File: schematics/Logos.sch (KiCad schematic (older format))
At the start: 10 parts

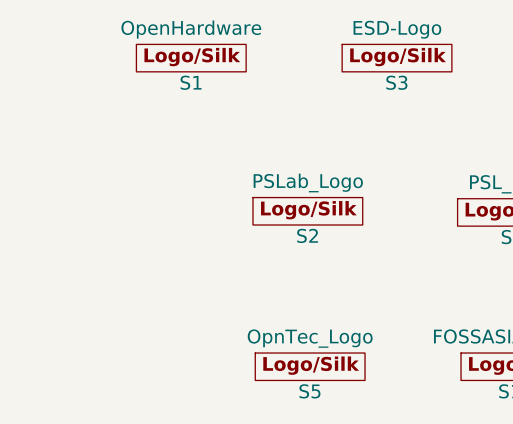
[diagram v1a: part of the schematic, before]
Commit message: feat: added ws2812b led
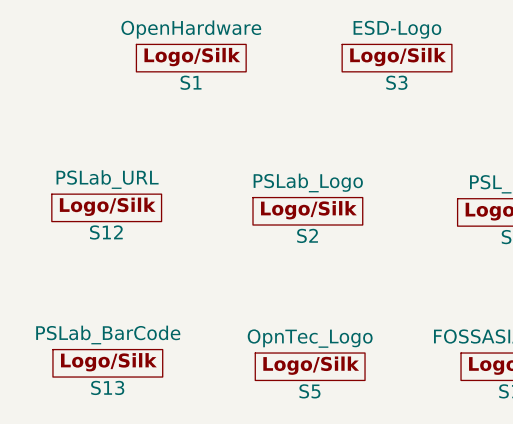
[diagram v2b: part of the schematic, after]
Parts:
- added S12: PSLab_URL, Custom_Components:PSLab_URL, symbol PSLab:Logos
- added S13: PSLab_BarCode, Custom_Components:Barcode, symbol PSLab:Logos
- S1: footprint Symbols:OSHW-Logo_5.7x6mm_SilkScreen -> Symbol:OSHW-Logo_5.7x6mm_SilkScreen
- S3: footprint Symbols:ESD-Logo_6.6x6mm_SilkScreen -> Symbol:ESD-Logo_6.6x6mm_SilkScreen
- S5: footprint Custom_Components:OpnTec_Logo -> Custom_Components:OpnTec_Logo_L
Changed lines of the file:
@@
 F 0 "S1" H 4560 2725 60  0000 C CNN
 F 1 "OpenHardware" H 4560 2965 60  0000 C CNN
-F 2 "Symbols:OSHW-Logo_5.7x6mm_SilkScreen" H 4560 2845 60  0001 C CNN
+F 2 "Symbol:OSHW-Logo_5.7x6mm_SilkScreen" H 4560 2845 60  0001 C CNN
 F 3 "" H 4560 2845 60  0001 C CNN
 	1    4560 2845
@@
 F 0 "S3" H 5460 2725 60  0000 C CNN
 F 1 "ESD-Logo" H 5460 2965 60  0000 C CNN
-F 2 "Symbols:ESD-Logo_6.6x6mm_SilkScreen" H 5460 2845 60  0001 C CNN
+F 2 "Symbol:ESD-Logo_6.6x6mm_SilkScreen" H 5460 2845 60  0001 C CNN
 F 3 "" H 5460 2845 60  0001 C CNN
 	1    5460 2845
@@
 F 0 "S5" H 5080 4075 60  0000 C CNN
 F 1 "OpnTec_Logo" H 5080 4315 60  0000 C CNN
-F 2 "Custom_Components:OpnTec_Logo" H 5080 4195 60  0001 C CNN
+F 2 "Custom_Components:OpnTec_Logo_L" H 5080 4195 60  0001 C CNN
 F 3 "" H 5080 4195 60  0001 C CNN
 	1    5080 4195
@@
 	1    0    0    -1
 $EndComp
+$Comp
+L PSLab:Logos S13
+U 1 1 5F7D714E
+P 4195 4180
+F 0 "S13" H 4195 4060 60  0000 C CNN
+F 1 "PSLab_BarCode" H 4195 4300 60  0000 C CNN
+F 2 "Custom_Components:Barcode" H 4195 4180 60  0001 C CNN
+F 3 "" H 4195 4180 60  0001 C CNN
+	1    4195 4180
+	1    0    0    -1
+$EndComp
+$Comp
+L PSLab:Logos S12
+U 1 1 5F7D7A3D
+P 4190 3500
+F 0 "S12" H 4190 3380 60  0000 C CNN
+F 1 "PSLab_URL" H 4190 3620 60  0000 C CNN
+F 2 "Custom_Components:PSLab_URL" H 4190 3500 60  0001 C CNN
+F 3 "" H 4190 3500 60  0001 C CNN
+	1    4190 3500
+	1    0    0    -1
+$EndComp

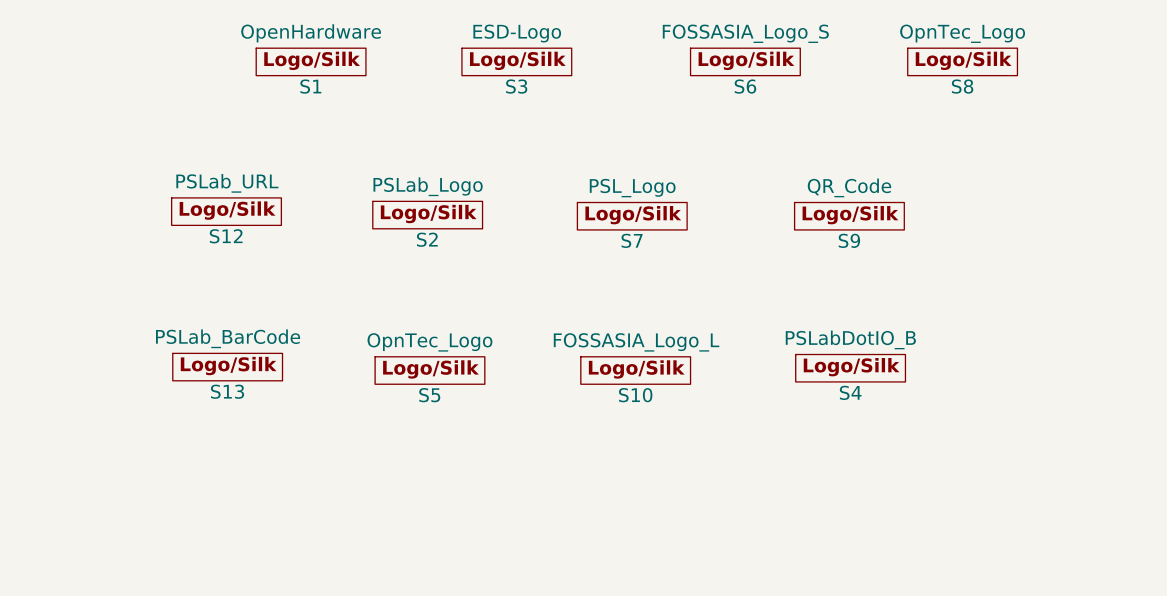
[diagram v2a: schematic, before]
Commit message: feat: enhanced bottom silk screen
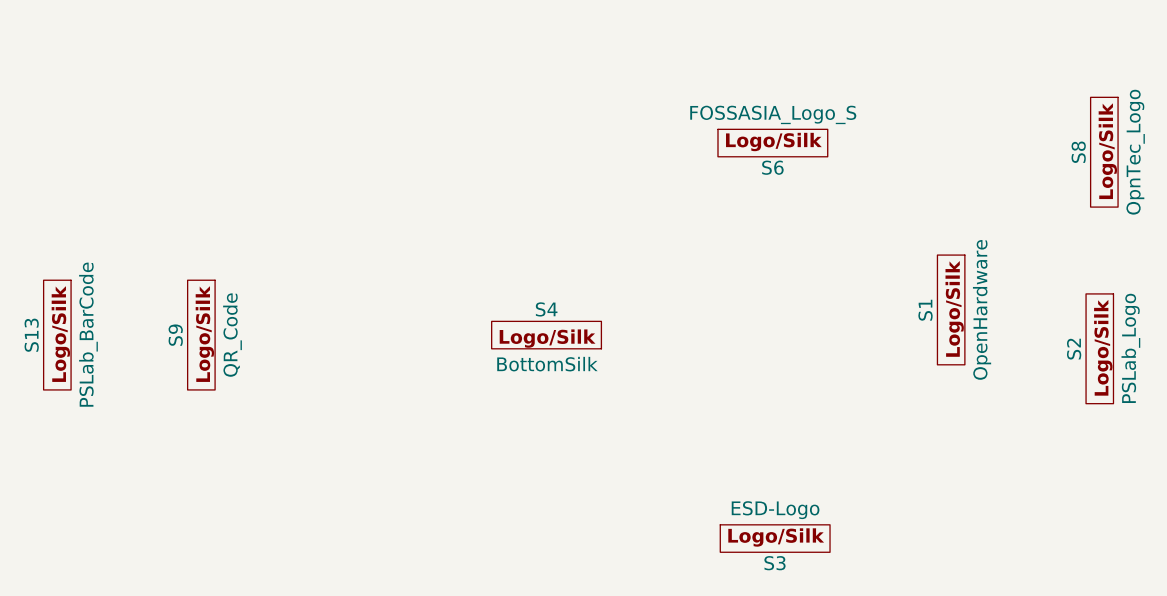
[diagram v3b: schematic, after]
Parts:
- removed S10: FOSSASIA_Logo_L, Custom_Components:FOSSASIA_LogoL, symbol PSLab:Logos
- removed S12: PSLab_URL, Custom_Components:PSLab_URL, symbol PSLab:Logos
- removed S5: OpnTec_Logo, Custom_Components:OpnTec_Logo_L, symbol PSLab:Logos
- removed S7: PSL_Logo, Custom_Components:PSL_Logo, symbol PSLab:Logos
- S4: value PSLabDotIO_B -> BottomSilk; footprint Custom_Components:PSLabDotIO4000 -> Custom_Components:PSLabRearSilk
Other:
- moved on the sheet: S1, S13, S2, S3, S6, S8, S9
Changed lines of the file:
@@
 L PSLab:Logos S1
 U 1 1 5C27C643
-P 4560 2845
-F 0 "S1" H 4560 2725 60  0000 C CNN
-F 1 "OpenHardware" H 4560 2965 60  0000 C CNN
-F 2 "Symbol:OSHW-Logo_5.7x6mm_SilkScreen" H 4560 2845 60  0001 C CNN
-F 3 "" H 4560 2845 60  0001 C CNN
-	1    4560 2845
-	1    0    0    -1
+P 7370 3940
+F 0 "S1" H 7370 3820 60  0000 C CNN
+F 1 "OpenHardware" H 7370 4060 60  0000 C CNN
+F 2 "Symbol:OSHW-Logo_5.7x6mm_SilkScreen" H 7370 3940 60  0001 C CNN
+F 3 "" H 7370 3940 60  0001 C CNN
+	1    7370 3940
+	0    1    1    0
 $EndComp
 $Comp
 L PSLab:Logos S3
 U 1 1 5C27C831
-P 5460 2845
-F 0 "S3" H 5460 2725 60  0000 C CNN
-F 1 "ESD-Logo" H 5460 2965 60  0000 C CNN
-F 2 "Symbol:ESD-Logo_6.6x6mm_SilkScreen" H 5460 2845 60  0001 C CNN
-F 3 "" H 5460 2845 60  0001 C CNN
-	1    5460 2845
+P 6590 4930
+F 0 "S3" H 6590 4810 60  0000 C CNN
+F 1 "ESD-Logo" H 6590 5050 60  0000 C CNN
+F 2 "Symbol:ESD-Logo_6.6x6mm_SilkScreen" H 6590 4930 60  0001 C CNN
+F 3 "" H 6590 4930 60  0001 C CNN
+	1    6590 4930
 	1    0    0    -1
 $EndComp
@@
 L PSLab:Logos S6
 U 1 1 5C27C867
-P 6460 2845
-F 0 "S6" H 6460 2725 60  0000 C CNN
-F 1 "FOSSASIA_Logo_S" H 6460 2965 60  0000 C CNN
-F 2 "Custom_Components:FOSSASIA_Logo" H 6460 2845 60  0001 C CNN
-F 3 "" H 6460 2845 60  0001 C CNN
-	1    6460 2845
+P 6580 3200
+F 0 "S6" H 6580 3080 60  0000 C CNN
+F 1 "FOSSASIA_Logo_S" H 6580 3320 60  0000 C CNN
+F 2 "Custom_Components:FOSSASIA_Logo" H 6580 3200 60  0001 C CNN
+F 3 "" H 6580 3200 60  0001 C CNN
+	1    6580 3200
 	1    0    0    -1
 $EndComp
@@
 L PSLab:Logos S8
 U 1 1 5C27C8A4
-P 7410 2845
-F 0 "S8" H 7410 2725 60  0000 C CNN
-F 1 "OpnTec_Logo" H 7410 2965 60  0000 C CNN
-F 2 "Custom_Components:OpnTec_Logo" H 7410 2845 60  0001 C CNN
-F 3 "" H 7410 2845 60  0001 C CNN
-	1    7410 2845
-	1    0    0    -1
+P 8040 3250
+F 0 "S8" H 8040 3130 60  0000 C CNN
+F 1 "OpnTec_Logo" H 8040 3370 60  0000 C CNN
+F 2 "Custom_Components:OpnTec_Logo" H 8040 3250 60  0001 C CNN
+F 3 "" H 8040 3250 60  0001 C CNN
+	1    8040 3250
+	0    1    1    0
 $EndComp
 $Comp
 L PSLab:Logos S2
 U 1 1 5C27C95E
-P 5070 3515
-F 0 "S2" H 5070 3395 60  0000 C CNN
-F 1 "PSLab_Logo" H 5070 3635 60  0000 C CNN
-F 2 "Custom_Components:PSLabDotIO" H 5070 3515 60  0001 C CNN
-F 3 "" H 5070 3515 60  0001 C CNN
-	1    5070 3515
-	1    0    0    -1
+P 8020 4110
+F 0 "S2" H 8020 3990 60  0000 C CNN
+F 1 "PSLab_Logo" H 8020 4230 60  0000 C CNN
+F 2 "Custom_Components:PSLabDotIO" H 8020 4110 60  0001 C CNN
+F 3 "" H 8020 4110 60  0001 C CNN
+	1    8020 4110
+	0    1    1    0
 $EndComp
 $Comp
-L PSLab:Logos S7
-U 1 1 5C27C96A
-P 5965 3520
-F 0 "S7" H 5965 3400 60  0000 C CNN
-F 1 "PSL_Logo" H 5965 3640 60  0000 C CNN
-F 2 "Custom_Components:PSL_Logo" H 5965 3520 60  0001 C CNN
-F 3 "" H 5965 3520 60  0001 C CNN
-	1    5965 3520
-	1    0    0    -1
+L PSLab:Logos S13
+U 1 1 5F7D714E
+P 3460 4050
+F 0 "S13" H 3460 3930 60  0000 C CNN
+F 1 "PSLab_BarCode" H 3460 4170 60  0000 C CNN
+F 2 "Custom_Components:Barcode" H 3460 4050 60  0001 C CNN
+F 3 "" H 3460 4050 60  0001 C CNN
+	1    3460 4050
+	0    1    1    0
 $EndComp
 $Comp
 L PSLab:Logos S9
 U 1 1 5C27C970
-P 6915 3520
-F 0 "S9" H 6915 3400 60  0000 C CNN
-F 1 "QR_Code" H 6915 3640 60  0000 C CNN
-F 2 "Custom_Components:Website_QR" H 6915 3520 60  0001 C CNN
-F 3 "" H 6915 3520 60  0001 C CNN
-	1    6915 3520
-	1    0    0    -1
-$EndComp
-$Comp
-L PSLab:Logos S5
-U 1 1 5C27C986
-P 5080 4195
-F 0 "S5" H 5080 4075 60  0000 C CNN
-F 1 "OpnTec_Logo" H 5080 4315 60  0000 C CNN
-F 2 "Custom_Components:OpnTec_Logo_L" H 5080 4195 60  0001 C CNN
-F 3 "" H 5080 4195 60  0001 C CNN
-	1    5080 4195
-	1    0    0    -1
-$EndComp
-$Comp
-L PSLab:Logos S10
-U 1 1 5C27CF8C
-P 5980 4195
-F 0 "S10" H 5980 4075 60  0000 C CNN
-F 1 "FOSSASIA_Logo_L" H 5980 4315 60  0000 C CNN
-F 2 "Custom_Components:FOSSASIA_LogoL" H 5980 4195 60  0001 C CNN
-F 3 "" H 5980 4195 60  0001 C CNN
-	1    5980 4195
-	1    0    0    -1
+P 4090 4050
+F 0 "S9" H 4090 3930 60  0000 C CNN
+F 1 "QR_Code" H 4090 4170 60  0000 C CNN
+F 2 "Custom_Components:Website_QR" H 4090 4050 60  0001 C CNN
+F 3 "" H 4090 4050 60  0001 C CNN
+	1    4090 4050
+	0    1    1    0
 $EndComp
 $Comp
 L PSLab:Logos S4
-U 1 1 5CB69B79
-P 6920 4185
-F 0 "S4" H 6920 4065 60  0000 C CNN
-F 1 "PSLabDotIO_B" H 6920 4305 60  0000 C CNN
-F 2 "Custom_Components:PSLabDotIO4000" H 6920 4185 60  0001 C CNN
-F 3 "" H 6920 4185 60  0001 C CNN
-	1    6920 4185
-	1    0    0    -1
-$EndComp
-$Comp
-L PSLab:Logos S13
-U 1 1 5F7D714E
-P 4195 4180
-F 0 "S13" H 4195 4060 60  0000 C CNN
-F 1 "PSLab_BarCode" H 4195 4300 60  0000 C CNN
-F 2 "Custom_Components:Barcode" H 4195 4180 60  0001 C CNN
-F 3 "" H 4195 4180 60  0001 C CNN
-	1    4195 4180
-	1    0    0    -1
-$EndComp
-$Comp
-L PSLab:Logos S12
-U 1 1 5F7D7A3D
-P 4190 3500
-F 0 "S12" H 4190 3380 60  0000 C CNN
-F 1 "PSLab_URL" H 4190 3620 60  0000 C CNN
-F 2 "Custom_Components:PSLab_URL" H 4190 3500 60  0001 C CNN
-F 3 "" H 4190 3500 60  0001 C CNN
-	1    4190 3500
-	1    0    0    -1
+U 1 1 5F925016
+P 5590 4060
+F 0 "S4" H 5590 3940 60  0000 C CNN
+F 1 "BottomSilk" H 5590 4180 60  0000 C CNN
+F 2 "Custom_Components:PSLabRearSilk" H 5590 4060 60  0001 C CNN
+F 3 "" H 5590 4060 60  0001 C CNN
+	1    5590 4060
+	-1   0    0    1
 $EndComp
 $EndSCHEMATC

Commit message: fix: courtyars, F2 fuse and RGB LED diode
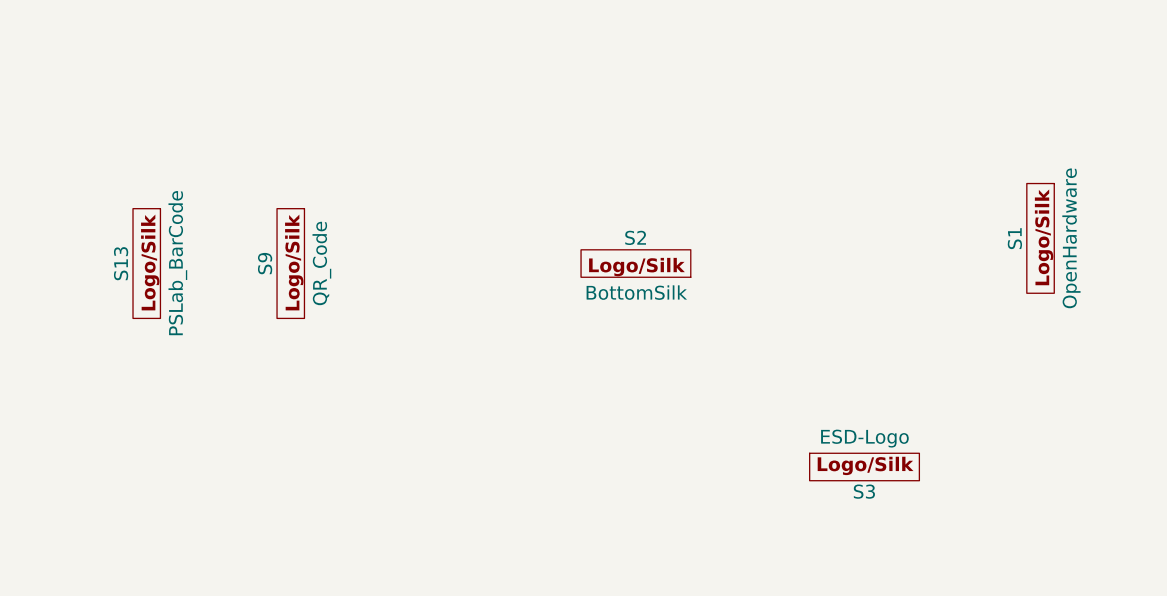
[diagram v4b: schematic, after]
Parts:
- removed S2: PSLab_Logo, Custom_Components:PSLabDotIO, symbol PSLab:Logos
- removed S6: FOSSASIA_Logo_S, Custom_Components:FOSSASIA_Logo, symbol PSLab:Logos
- removed S8: OpnTec_Logo, Custom_Components:OpnTec_Logo, symbol PSLab:Logos
- renumbered S4 to S2
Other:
- moved on the sheet: S1, S13, S2, S3, S9
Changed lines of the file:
@@
 L PSLab:Logos S1
 U 1 1 5C27C643
-P 7370 3940
-F 0 "S1" H 7370 3820 60  0000 C CNN
-F 1 "OpenHardware" H 7370 4060 60  0000 C CNN
-F 2 "Symbol:OSHW-Logo_5.7x6mm_SilkScreen" H 7370 3940 60  0001 C CNN
-F 3 "" H 7370 3940 60  0001 C CNN
-	1    7370 3940
+P 7761 3627
+F 0 "S1" H 7761 3507 60  0000 C CNN
+F 1 "OpenHardware" H 7761 3747 60  0000 C CNN
+F 2 "Symbol:OSHW-Logo_5.7x6mm_SilkScreen" H 7761 3627 60  0001 C CNN
+F 3 "" H 7761 3627 60  0001 C CNN
+	1    7761 3627
 	0    1    1    0
 $EndComp
@@
 L PSLab:Logos S3
 U 1 1 5C27C831
-P 6590 4930
-F 0 "S3" H 6590 4810 60  0000 C CNN
-F 1 "ESD-Logo" H 6590 5050 60  0000 C CNN
-F 2 "Symbol:ESD-Logo_6.6x6mm_SilkScreen" H 6590 4930 60  0001 C CNN
-F 3 "" H 6590 4930 60  0001 C CNN
-	1    6590 4930
+P 6981 4617
+F 0 "S3" H 6981 4497 60  0000 C CNN
+F 1 "ESD-Logo" H 6981 4737 60  0000 C CNN
+F 2 "Symbol:ESD-Logo_6.6x6mm_SilkScreen" H 6981 4617 60  0001 C CNN
+F 3 "" H 6981 4617 60  0001 C CNN
+	1    6981 4617
 	1    0    0    -1
-$EndComp
-$Comp
-L PSLab:Logos S6
-U 1 1 5C27C867
-P 6580 3200
-F 0 "S6" H 6580 3080 60  0000 C CNN
-F 1 "FOSSASIA_Logo_S" H 6580 3320 60  0000 C CNN
-F 2 "Custom_Components:FOSSASIA_Logo" H 6580 3200 60  0001 C CNN
-F 3 "" H 6580 3200 60  0001 C CNN
-	1    6580 3200
-	1    0    0    -1
-$EndComp
-$Comp
-L PSLab:Logos S8
-U 1 1 5C27C8A4
-P 8040 3250
-F 0 "S8" H 8040 3130 60  0000 C CNN
-F 1 "OpnTec_Logo" H 8040 3370 60  0000 C CNN
-F 2 "Custom_Components:OpnTec_Logo" H 8040 3250 60  0001 C CNN
-F 3 "" H 8040 3250 60  0001 C CNN
-	1    8040 3250
-	0    1    1    0
-$EndComp
-$Comp
-L PSLab:Logos S2
-U 1 1 5C27C95E
-P 8020 4110
-F 0 "S2" H 8020 3990 60  0000 C CNN
-F 1 "PSLab_Logo" H 8020 4230 60  0000 C CNN
-F 2 "Custom_Components:PSLabDotIO" H 8020 4110 60  0001 C CNN
-F 3 "" H 8020 4110 60  0001 C CNN
-	1    8020 4110
-	0    1    1    0
 $EndComp
 $Comp
 L PSLab:Logos S13
 U 1 1 5F7D714E
-P 3460 4050
-F 0 "S13" H 3460 3930 60  0000 C CNN
-F 1 "PSLab_BarCode" H 3460 4170 60  0000 C CNN
-F 2 "Custom_Components:Barcode" H 3460 4050 60  0001 C CNN
-F 3 "" H 3460 4050 60  0001 C CNN
-	1    3460 4050
+P 3851 3737
+F 0 "S13" H 3851 3617 60  0000 C CNN
+F 1 "PSLab_BarCode" H 3851 3857 60  0000 C CNN
+F 2 "Custom_Components:Barcode" H 3851 3737 60  0001 C CNN
+F 3 "" H 3851 3737 60  0001 C CNN
+	1    3851 3737
 	0    1    1    0
 $EndComp
@@
 L PSLab:Logos S9
 U 1 1 5C27C970
-P 4090 4050
-F 0 "S9" H 4090 3930 60  0000 C CNN
-F 1 "QR_Code" H 4090 4170 60  0000 C CNN
-F 2 "Custom_Components:Website_QR" H 4090 4050 60  0001 C CNN
-F 3 "" H 4090 4050 60  0001 C CNN
-	1    4090 4050
+P 4481 3737
+F 0 "S9" H 4481 3617 60  0000 C CNN
+F 1 "QR_Code" H 4481 3857 60  0000 C CNN
+F 2 "Custom_Components:Website_QR" H 4481 3737 60  0001 C CNN
+F 3 "" H 4481 3737 60  0001 C CNN
+	1    4481 3737
 	0    1    1    0
 $EndComp
 $Comp
-L PSLab:Logos S4
+L PSLab:Logos S2
 U 1 1 5F925016
-P 5590 4060
-F 0 "S4" H 5590 3940 60  0000 C CNN
-F 1 "BottomSilk" H 5590 4180 60  0000 C CNN
-F 2 "Custom_Components:PSLabRearSilk" H 5590 4060 60  0001 C CNN
-F 3 "" H 5590 4060 60  0001 C CNN
-	1    5590 4060
+P 5981 3747
+F 0 "S2" H 5981 3627 60  0000 C CNN
+F 1 "BottomSilk" H 5981 3867 60  0000 C CNN
+F 2 "Custom_Components:PSLabRearSilk" H 5981 3747 60  0001 C CNN
+F 3 "" H 5981 3747 60  0001 C CNN
+	1    5981 3747
 	-1   0    0    1
 $EndComp

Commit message: feat: bom generator and updated project to support bom generator
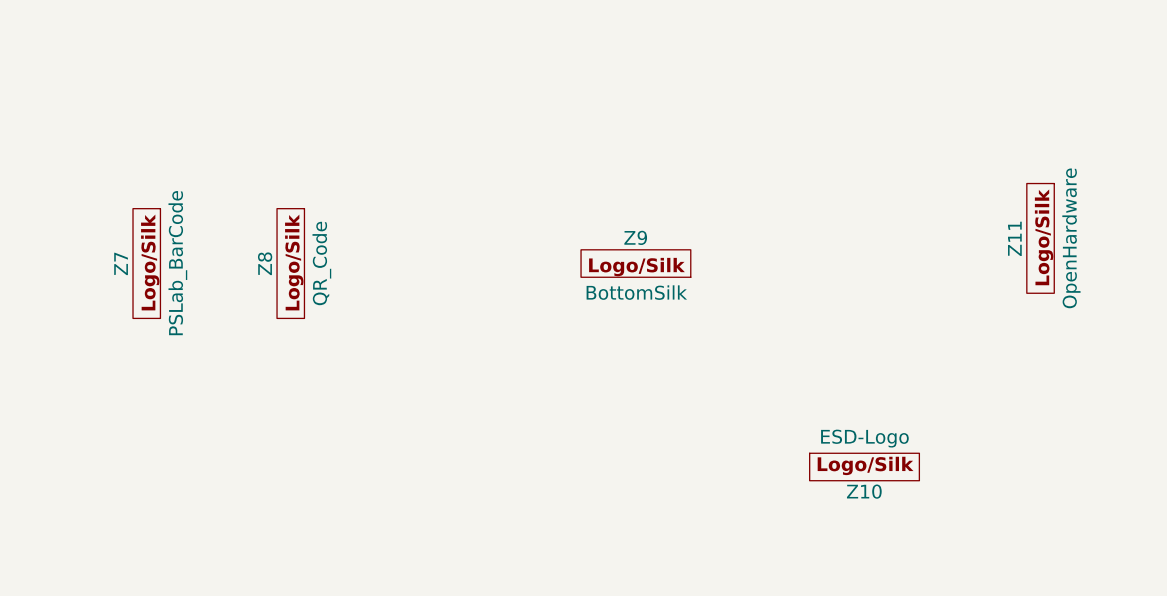
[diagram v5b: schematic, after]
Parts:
- Z7: renamed from S13; footprint Custom_Components:Barcode -> PSLab:Barcode
- Z8: renamed from S9; footprint Custom_Components:Website_QR -> PSLab:Website_QR
- Z9: renamed from S2; footprint Custom_Components:PSLabRearSilk -> PSLab:PSLabRearSilk
- renumbered S3 to Z10, S1 to Z11
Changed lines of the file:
@@
 $EndDescr
 $Comp
-L PSLab:Logos S1
+L PSLab:Logos Z11
 U 1 1 5C27C643
 P 7761 3627
-F 0 "S1" H 7761 3507 60  0000 C CNN
+F 0 "Z11" H 7761 3507 60  0000 C CNN
 F 1 "OpenHardware" H 7761 3747 60  0000 C CNN
 F 2 "Symbol:OSHW-Logo_5.7x6mm_SilkScreen" H 7761 3627 60  0001 C CNN
@@
 $EndComp
 $Comp
-L PSLab:Logos S3
+L PSLab:Logos Z10
 U 1 1 5C27C831
 P 6981 4617
-F 0 "S3" H 6981 4497 60  0000 C CNN
+F 0 "Z10" H 6981 4497 60  0000 C CNN
 F 1 "ESD-Logo" H 6981 4737 60  0000 C CNN
 F 2 "Symbol:ESD-Logo_6.6x6mm_SilkScreen" H 6981 4617 60  0001 C CNN
@@
 $EndComp
 $Comp
-L PSLab:Logos S13
+L PSLab:Logos Z7
 U 1 1 5F7D714E
 P 3851 3737
-F 0 "S13" H 3851 3617 60  0000 C CNN
+F 0 "Z7" H 3851 3617 60  0000 C CNN
 F 1 "PSLab_BarCode" H 3851 3857 60  0000 C CNN
-F 2 "Custom_Components:Barcode" H 3851 3737 60  0001 C CNN
+F 2 "PSLab:Barcode" H 3851 3737 60  0001 C CNN
 F 3 "" H 3851 3737 60  0001 C CNN
 	1    3851 3737
@@
 $EndComp
 $Comp
-L PSLab:Logos S9
+L PSLab:Logos Z8
 U 1 1 5C27C970
 P 4481 3737
-F 0 "S9" H 4481 3617 60  0000 C CNN
+F 0 "Z8" H 4481 3617 60  0000 C CNN
 F 1 "QR_Code" H 4481 3857 60  0000 C CNN
-F 2 "Custom_Components:Website_QR" H 4481 3737 60  0001 C CNN
+F 2 "PSLab:Website_QR" H 4481 3737 60  0001 C CNN
 F 3 "" H 4481 3737 60  0001 C CNN
 	1    4481 3737
@@
 $EndComp
 $Comp
-L PSLab:Logos S2
+L PSLab:Logos Z9
 U 1 1 5F925016
 P 5981 3747
-F 0 "S2" H 5981 3627 60  0000 C CNN
+F 0 "Z9" H 5981 3627 60  0000 C CNN
 F 1 "BottomSilk" H 5981 3867 60  0000 C CNN
-F 2 "Custom_Components:PSLabRearSilk" H 5981 3747 60  0001 C CNN
+F 2 "PSLab:PSLabRearSilk" H 5981 3747 60  0001 C CNN
 F 3 "" H 5981 3747 60  0001 C CNN
 	1    5981 3747
